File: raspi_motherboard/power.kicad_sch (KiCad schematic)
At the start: 30 parts, among them J3 Conn_01x03, U3 TPS563200

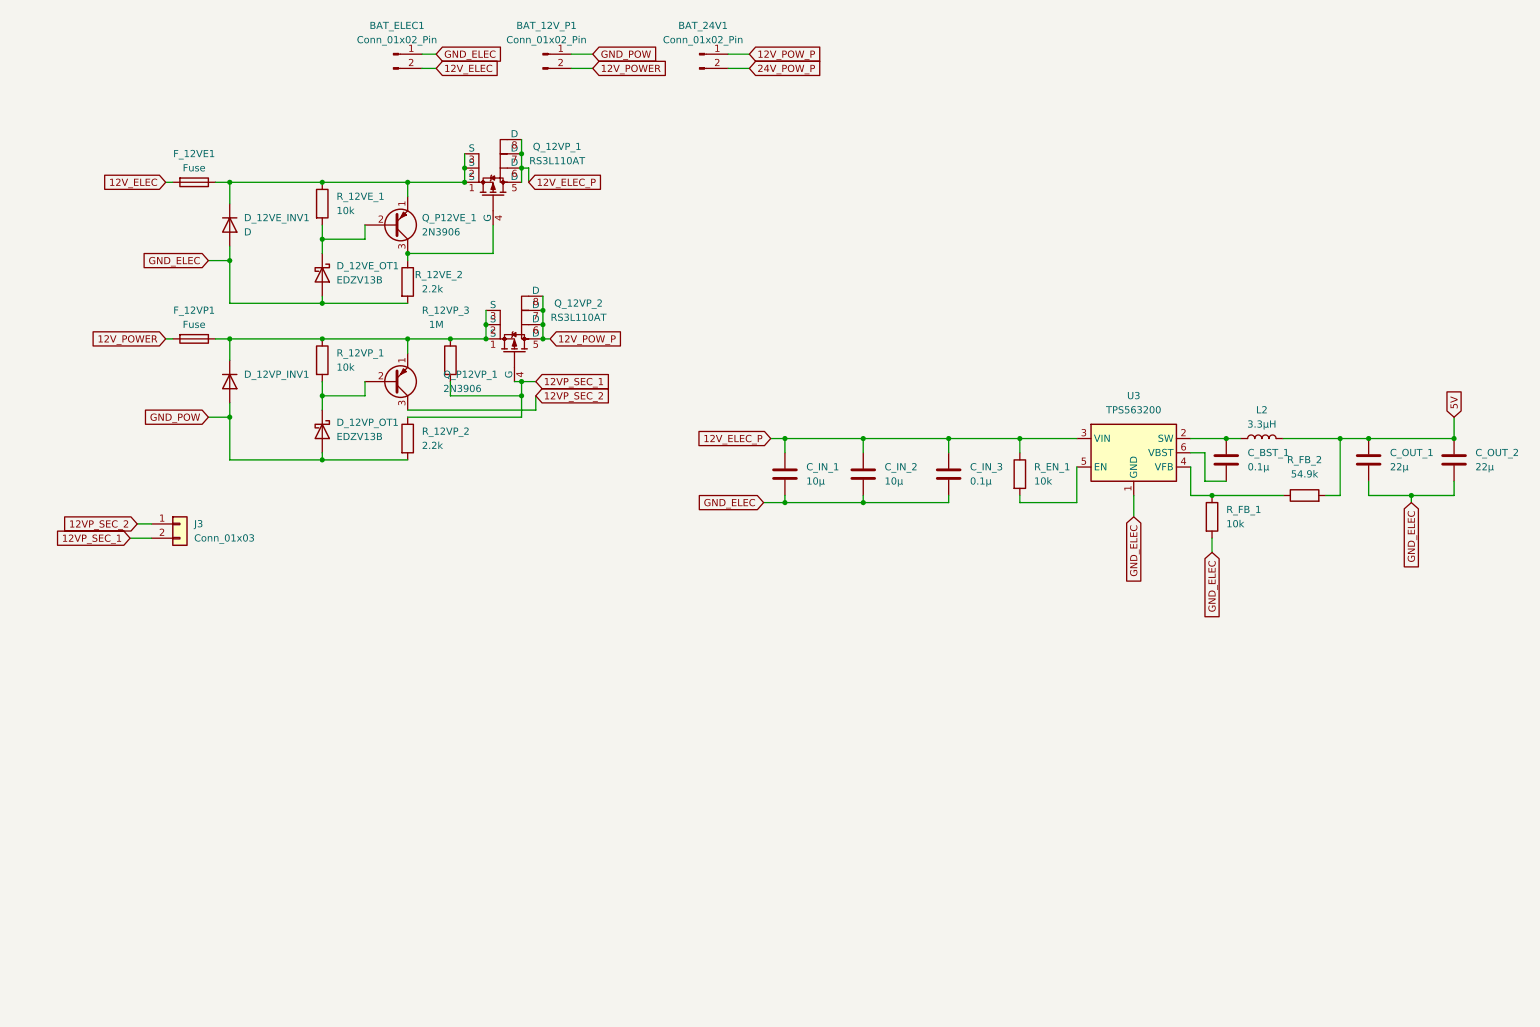
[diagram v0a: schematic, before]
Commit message: V2 of the board: 24 Volt power
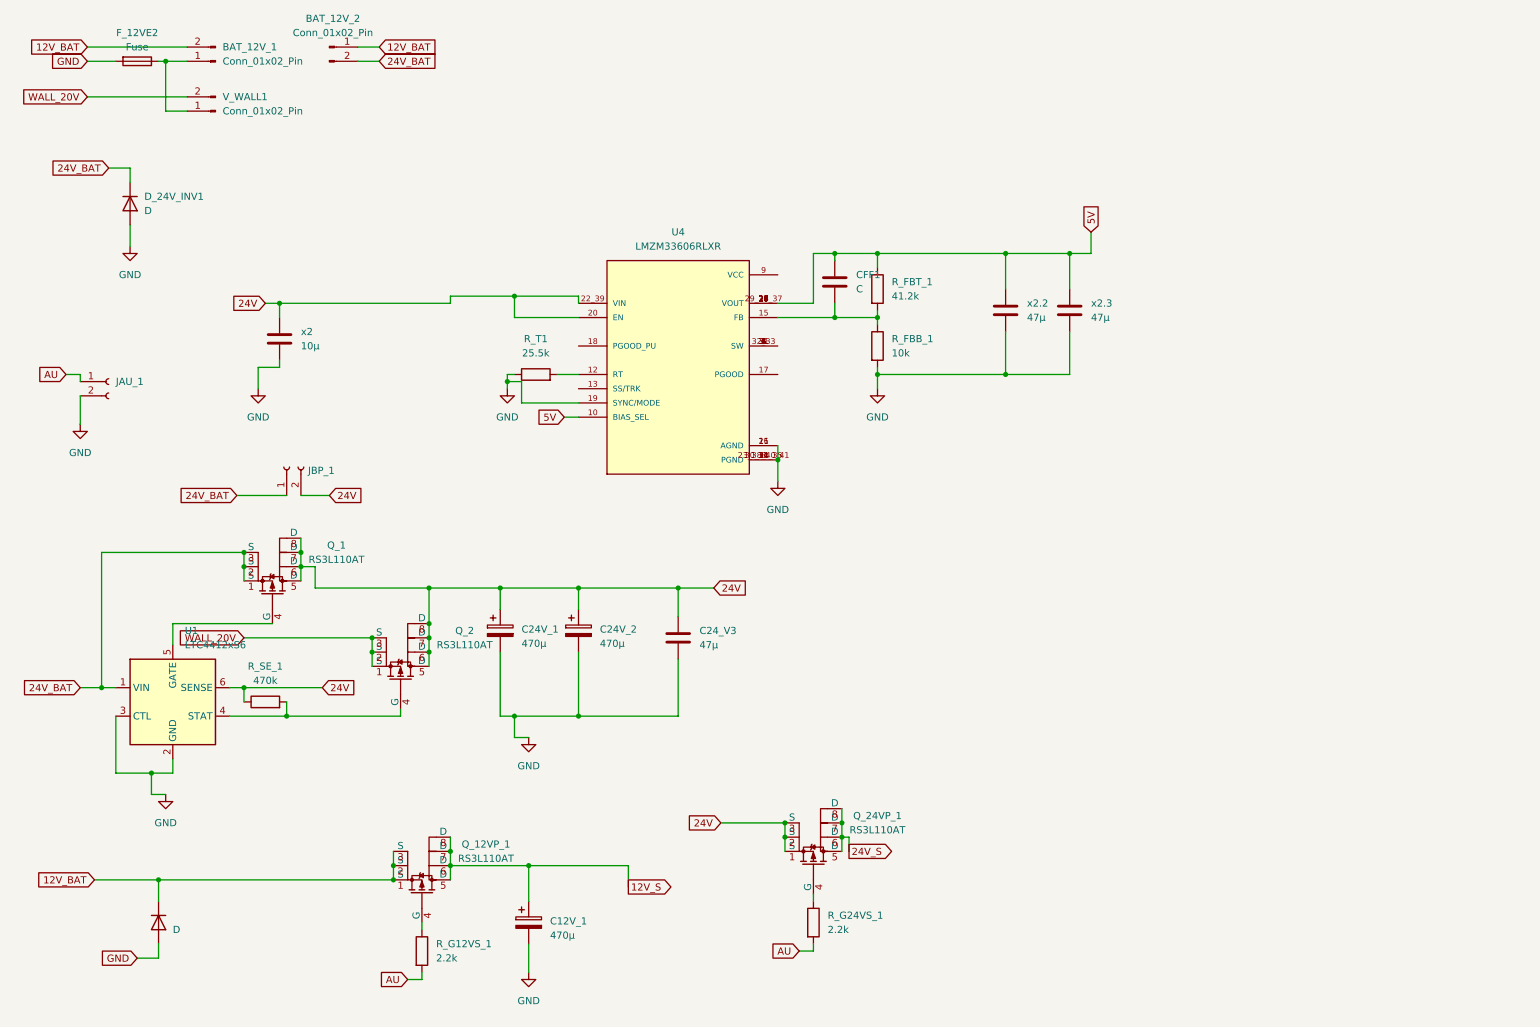
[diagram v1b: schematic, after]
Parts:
- removed BAT_24V1: Conn_01x02_Pin, Connector_Phoenix_MC:PhoenixContact_MCV_1,5_2-G-3.81_1x02_P3.81mm_Vertical, symbol Connector:Conn_01x02_Pin
- removed C_BST_1, C_IN_3: 0.1µ, Capacitor_SMD:C_0603_1608Metric, symbol Device:C
- removed C_IN_2: 10µ, Capacitor_SMD:C_1206_3216Metric, symbol Device:C
- removed C_OUT_1, C_OUT_2: 22µ, Capacitor_SMD:C_0603_1608Metric, symbol Device:C
- removed D_12VE_OT1, D_12VP_OT1: EDZV13B, Diode_SMD:D_SOD-523, symbol Device:D_Schottky
- removed D_12VP_INV1: ~, Diode_SMD:D_SOD-123F, symbol Device:D
- removed F_12VE1, F_12VP1: Fuse, Fuse:Fuse_Littelfuse-NANO2-451_453, symbol Device:Fuse
- removed J3: Conn_01x03, Connector_PinSocket_2.54mm:PinSocket_1x02_P2.54mm_Vertical, symbol Connector_Generic:Conn_01x02
- removed L2: 3.3µH, powerboard:VLS4020CX-H, symbol Device:L
- removed Q_12VP_2: RS3L110AT, Package_SO:SOP-8_3.76x4.96mm_P1.27mm, symbol Simulation_SPICE:PMOS
- removed Q_P12VE_1, Q_P12VP_1: 2N3906, Package_TO_SOT_SMD:SOT-23, symbol Transistor_BJT:2N3906
- removed R_12VE_1, R_12VP_1, R_EN_1, R_FB_1: 10k, Resistor_SMD:R_0603_1608Metric, symbol Device:R
- removed R_12VE_2, R_12VP_2: 2.2k, Resistor_SMD:R_0603_1608Metric, symbol Device:R
- removed R_12VP_3: 1M, Resistor_SMD:R_0603_1608Metric, symbol Device:R
- removed R_FB_2: 54.9k, Resistor_SMD:R_0603_1608Metric, symbol Device:R
- removed U3: TPS563200, Package_TO_SOT_SMD:SOT-23-6, symbol Regulator_Switching:TPS563200
- added C12V_1, C24V_1, C24V_2: 470µ, powerboard:CP_Panasonic FN Series G size, symbol Device:C_Polarized
- added C24_V3, x2.2, x2.3: 47µ, Capacitor_SMD:C_1210_3225Metric, symbol Device:C
- added CFF1: C, Capacitor_SMD:C_0603_1608Metric, symbol Device:C
- added D_24V_INV1: D, Diode_SMD:D_SOD-123F, symbol Device:D
- added F_12VE2: Fuse, kicad libs:LittleFuse 154 holder, symbol Device:Fuse
- added JAU_1, JBP_1: Conn_01x02_Socket, Connector_PinSocket_1.00mm:PinSocket_1x02_P1.00mm_Vertical, symbol Connector:Conn_01x02_Socket
- added Q_1, Q_2, Q_24VP_1: RS3L110AT, Package_SO:SOP-8_3.76x4.96mm_P1.27mm, symbol Simulation_SPICE:PMOS
- added R_FBB_1: 10k, Resistor_SMD:R_0603_1608Metric, symbol Device:R
- added R_FBT_1: 41.2k, Resistor_SMD:R_0603_1608Metric, symbol Device:R
- added R_G12VS_1, R_G24VS_1: 2.2k, Resistor_SMD:R_0603_1608Metric, symbol Device:R
- added R_SE_1: 470k, Resistor_SMD:R_0603_1608Metric, symbol Device:R
- added R_T1: 25.5k, Resistor_SMD:R_0603_1608Metric, symbol Device:R
- added U1: LTC4412xS6, Package_TO_SOT_SMD:TSOT-23-6, symbol Power_Management:LTC4412xS6
- added U4: LMZM33606RLXR, powerboard:IC_LMZM33606RLXR, symbol LMZM33606:LMZM33606RLXR
- added V_WALL1: Conn_01x02_Pin, Connector_Phoenix_MC:PhoenixContact_MCV_1,5_2-G-3.81_1x02_P3.81mm_Vertical, symbol Connector:Conn_01x02_Pin
- x2: renamed from C_IN_1; footprint Capacitor_SMD:C_1206_3216Metric -> Capacitor_SMD:C_1210_3225Metric
- renumbered BAT_ELEC1 to BAT_12V_1, BAT_12V_P1 to BAT_12V_2, D_12VE_INV1 to D_12V_INV1
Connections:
- net 12V_ELEC is gone; now on net 12V_BAT: BAT_12V_1.2 (Pin_2)
- net GND_POW is gone; now on net 12V_BAT: BAT_12V_2.1 (Pin_1)
- net 5V: now also CFF1.1, R_FBT_1.1, U4.10 (BIAS_SEL), U4.24 (VOUT), U4.25 (VOUT), U4.26 (VOUT), U4.27 (VOUT), U4.28 (VOUT), U4.29_36_37 (VOUT), x2.2.1, x2.3.1
- net 12V_BAT: now reaches D_12V_INV1.1 (K), Q_12VP_1.1 (S), Q_12VP_1.2 (S), Q_12VP_1.3 (S)
- net at Q_12VP_1.4 (G): now also R_G12VS_1.1
- net 12V_ELEC_P renamed 12V_S
- net 12V_S: now also C12V_1.1; no longer x2.1
- net 12V_POWER renamed 24V_BAT
- net 24V_BAT: now also D_24V_INV1.1 (K), JBP_1.1 (Pin_1), Q_1.1 (S), Q_1.2 (S), Q_1.3 (S), U1.1 (VIN)
- net GND_ELEC renamed GND
- net GND: now also C12V_1.2, C24V_1.2, C24V_2.2, C24_V3.2, D_24V_INV1.2 (A), F_12VE2.2, JAU_1.2 (Pin_2), R_FBB_1.2, R_T1.1, U1.2 (GND), U1.3 (CTL), U4.11 (PGND), U4.16 (AGND), U4.19 (SYNC/MODE), U4.21 (AGND), U4.23_38_40_41 (PGND), U4.30_34_35 (PGND), U4.8 (PGND), x2.2.2, x2.3.2; no longer BAT_12V_1.1 (Pin_1)
- new net: CFF1.2, R_FBB_1.1, R_FBT_1.2, U4.15 (FB)
- new net: Q_24VP_1.4 (G), R_G24VS_1.1
- new net: Q_2.4 (G), R_SE_1.2, U1.4 (STAT)
- new net: R_T1.2, U4.12 (RT)
- new net: BAT_12V_1.1 (Pin_1), F_12VE2.1, V_WALL1.1 (Pin_1)
- new net: U4.1 (SW), U4.2 (SW), U4.3 (SW), U4.31 (SW), U4.32_33 (SW), U4.4 (SW), U4.5 (SW), U4.6 (SW)
- new net: Q_1.4 (G), U1.5 (GATE)
- new net 24V: C24V_1.1, C24V_2.1, C24_V3.1, JBP_1.2 (Pin_2), Q_1.5 (D), Q_1.6 (D), Q_1.7 (D), Q_1.8 (D), Q_2.5 (D), Q_2.6 (D), Q_2.7 (D), Q_2.8 (D), Q_24VP_1.1 (S), Q_24VP_1.2 (S), Q_24VP_1.3 (S), R_SE_1.1, U1.6 (SENSE), U4.20 (EN), U4.22_39 (VIN), x2.1
- new net 24V_S: Q_24VP_1.5 (D), Q_24VP_1.6 (D), Q_24VP_1.7 (D), Q_24VP_1.8 (D)
- new net AU: JAU_1.1 (Pin_1), R_G12VS_1.2, R_G24VS_1.2
- new net WALL_20V: Q_2.1 (S), Q_2.2 (S), Q_2.3 (S), V_WALL1.2 (Pin_2)
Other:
- moved on the sheet: BAT_12V_1, BAT_12V_2, Q_12VP_1, x2

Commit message: Routed
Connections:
- net 12V_S: no longer C12V_1.1
- net GND: no longer R_FBB_1.2, R_T1.1, U4.16 (AGND), U4.19 (SYNC/MODE), U4.21 (AGND)
- net SW: now reaches U4.1 (SW), U4.2 (SW), U4.3 (SW), U4.31 (SW), U4.32_33 (SW), U4.4 (SW), U4.5 (SW), U4.6 (SW)
- net 12V_BAT renamed 12V
- net 12V: now also C12V_1.1
- new net AGND: R_FBB_1.2, R_T1.1, U4.16 (AGND), U4.19 (SYNC/MODE), U4.21 (AGND)
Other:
- moved on the sheet: C12V_1

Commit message: Changing connectors
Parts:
- JAU_1: footprint Connector_PinSocket_1.00mm:PinSocket_1x02_P1.00mm_Vertical -> Connector_JST:JST_PH_B2B-PH-K_1x02_P2.00mm_Vertical
- JBP_1: footprint Connector_PinSocket_1.00mm:PinSocket_1x02_P1.00mm_Vertical -> Connector_PinHeader_1.27mm:PinHeader_1x02_P1.27mm_Vertical
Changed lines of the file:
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@@
 			)
 		)
-		(property "Footprint" "Connector_PinSocket_1.00mm:PinSocket_1x02_P1.00mm_Vertical"
+		(property "Footprint" "Connector_JST:JST_PH_B2B-PH-K_1x02_P2.00mm_Vertical"
 			(at 31.75 78.74 0)
 			(effects
@@
 			)
 		)
-		(property "Footprint" "Connector_PinSocket_1.00mm:PinSocket_1x02_P1.00mm_Vertical"
+		(property "Footprint" "Connector_PinHeader_1.27mm:PinHeader_1x02_P1.27mm_Vertical"
 			(at 63.5 93.98 0)
 			(effects

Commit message: Production version
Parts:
- CFF1: value C -> 58pF
- JBP_1: footprint Connector_PinHeader_1.27mm:PinHeader_1x02_P1.27mm_Vertical -> Connector_PinSocket_2.00mm:PinSocket_1x02_P2.00mm_Vertical
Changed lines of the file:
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@@
 			)
 		)
-		(property "Footprint" "Connector_PinHeader_1.27mm:PinHeader_1x02_P1.27mm_Vertical"
+		(property "Footprint" "Connector_PinSocket_2.00mm:PinSocket_1x02_P2.00mm_Vertical"
 			(at 63.5 93.98 0)
 			(effects
@@
 			)
 		)
-		(property "Value" "C"
+		(property "Value" "58pF"
 			(at 165.1 62.2299 0)
 			(effects
